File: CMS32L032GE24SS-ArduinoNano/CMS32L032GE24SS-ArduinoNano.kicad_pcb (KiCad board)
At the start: 2 copper layers, 18 x 43.2 mm, 20 parts, among them J101 MCU Right Side, J102 MCU Left Side, J105 Connection to DAPLink Board, U101 CMS32L032GE24SS, U301 AP2127K-ADJ

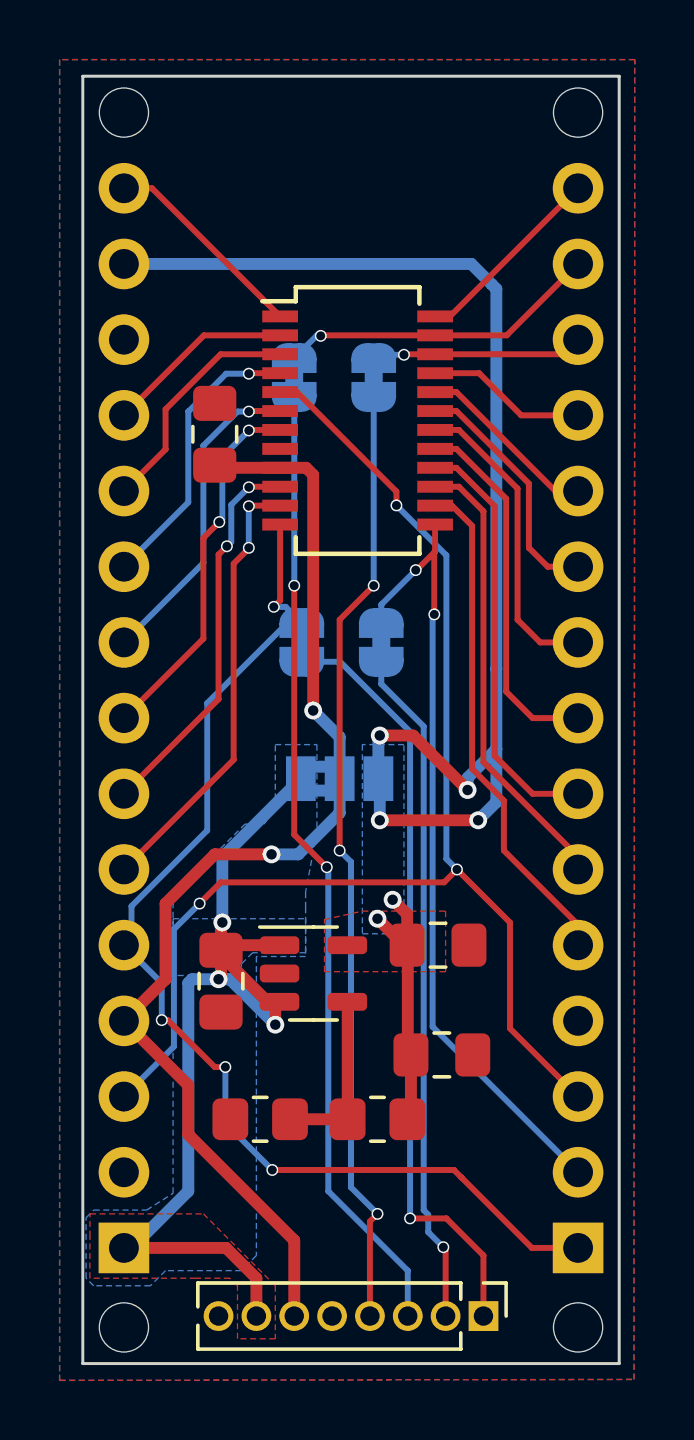
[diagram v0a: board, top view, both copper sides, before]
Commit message: added TEXT silkscreens
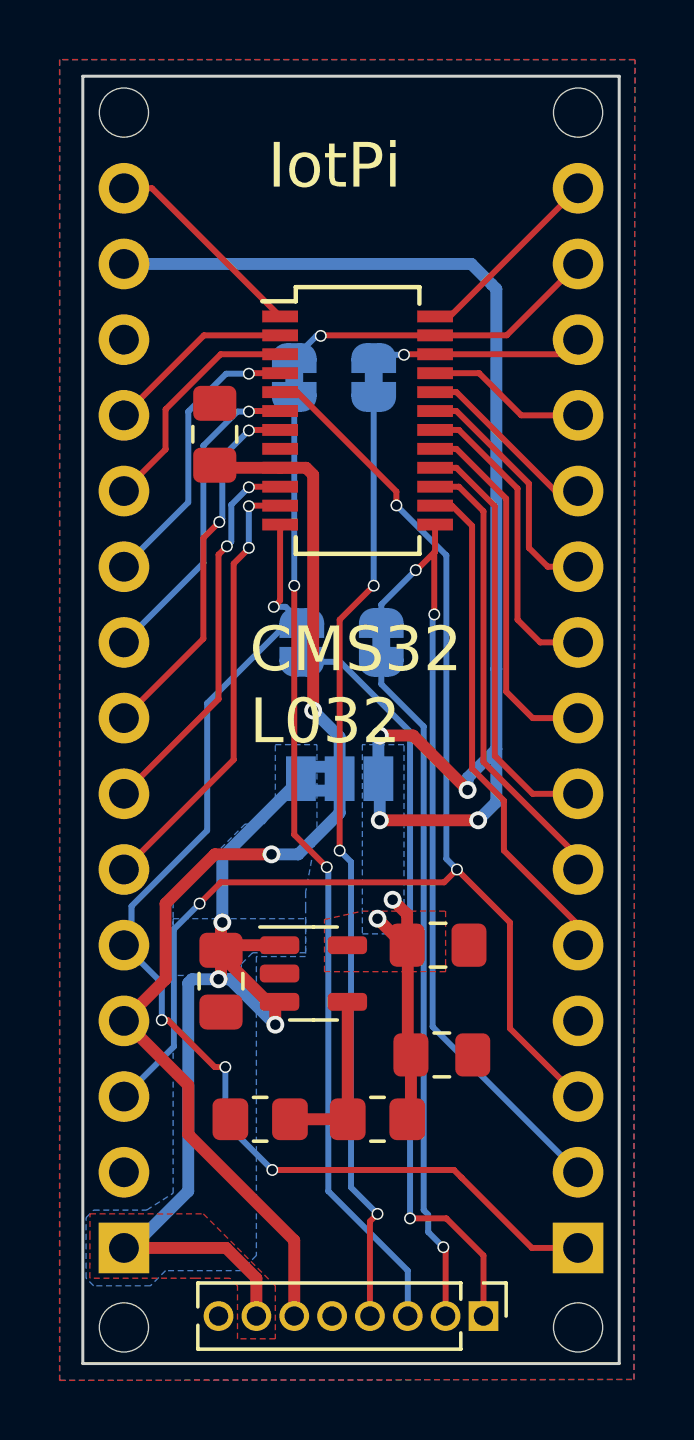
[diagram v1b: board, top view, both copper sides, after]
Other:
- board text added: "CMS32 L032"
- board text added: "GND"
- board text added: "IotPi"
- board text added: "RX Jumper"
- board text added: "RegV_{OUT}"
- board text added: "TX Jumper"
- board text added: "V_{IN}"
- board text added: "V_{MCU}"
- board text added: "Vol Jumper"
- board text added: "X"
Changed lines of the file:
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@@
   (gr_rect locked (start 91.694 49.971) (end 106.934 90.611)
     (stroke (width 0.1) (type default)) (fill none) (layer "F.Fab"))
+  (gr_text "GND" (at 105.0036 81.3308) (layer "B.SilkS")
+    (effects (font (size 1.5 1.5) (thickness 0.1)) (justify left bottom mirror))
+  )
+  (gr_text "GND" (at 97.9932 86.36) (layer "B.SilkS")
+    (effects (font (size 1.5 1.5) (thickness 0.1)) (justify left bottom mirror))
+  )
+  (gr_text "X" (at 94.742 58.1152) (layer "B.SilkS")
+    (effects (font (size 1 1) (thickness 0.1)) (justify left bottom mirror))
+  )
+  (gr_text "RX Jumper" (at 103.5812 64.8716 90) (layer "B.SilkS")
+    (effects (font (size 1 1) (thickness 0.1)) (justify left bottom mirror))
+  )
+  (gr_text "Vol Jumper" (at 95.3516 74.3204 180) (layer "B.SilkS")
+    (effects (font (size 1 1) (thickness 0.1)) (justify left bottom mirror))
+  )
+  (gr_text "RegV_{OUT}" (at 99.6696 55.4736) (layer "B.SilkS")
+    (effects (font (size 1 1) (thickness 0.1)) (justify left bottom mirror))
+  )
+  (gr_text "TX Jumper" (at 96.1136 64.9224 90) (layer "B.SilkS")
+    (effects (font (size 1 1) (thickness 0.1)) (justify left bottom mirror))
+  )
+  (gr_text "V_{MCU}" (at 98.552 81.2292) (layer "B.SilkS")
+    (effects (font (size 1.5 1.5) (thickness 0.1)) (justify left bottom mirror))
+  )
+  (gr_text "V_{IN}" (at 96.6216 88.7984) (layer "B.SilkS")
+    (effects (font (size 1.5 1.5) (thickness 0.1)) (justify left bottom mirror))
+  )
+  (gr_text "CMS32\nL032" (at 95.9104 71.2216) (layer "F.SilkS")
+    (effects (font (size 1.5 1.5) (thickness 0.1)) (justify left bottom))
+  )
+  (gr_text "IotPi" (at 96.52 52.578) (layer "F.SilkS")
+    (effects (font (size 1.5 1.5) (thickness 0.1)) (justify left bottom))
+  )
   (dimension (type aligned) (layer "B.Cu")
     (pts (xy 90.314 91.891) (xy 90.314 48.691))

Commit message: fix HuaQiu DFM issues
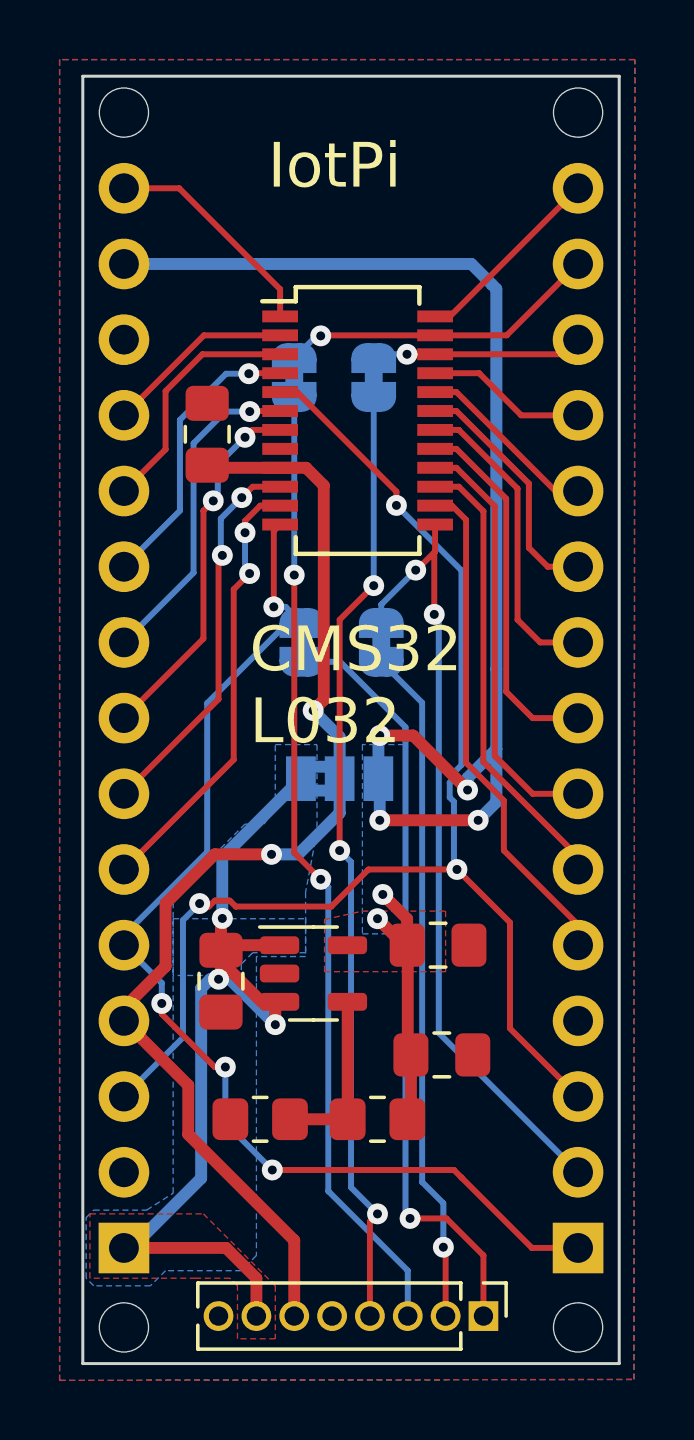
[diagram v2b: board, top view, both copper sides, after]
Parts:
- moved C101 0.25 mm to (94.5, 60.7)
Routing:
- net /CMS32L032GE24SS/MCU_PIN_RESET: track 44.8 -> 45.3 mm
- net /MCU_V_{IN}: track 39.0 -> 39.6 mm
- net /CMS32L032GE24SS/MCU_PIN_1: track 7.02 -> 7.56 mm
